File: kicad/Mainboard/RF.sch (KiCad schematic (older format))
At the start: 97 parts, among them J7 Antenna, T1 AFT05MS004NT1, U5 HMC546MS8GETR

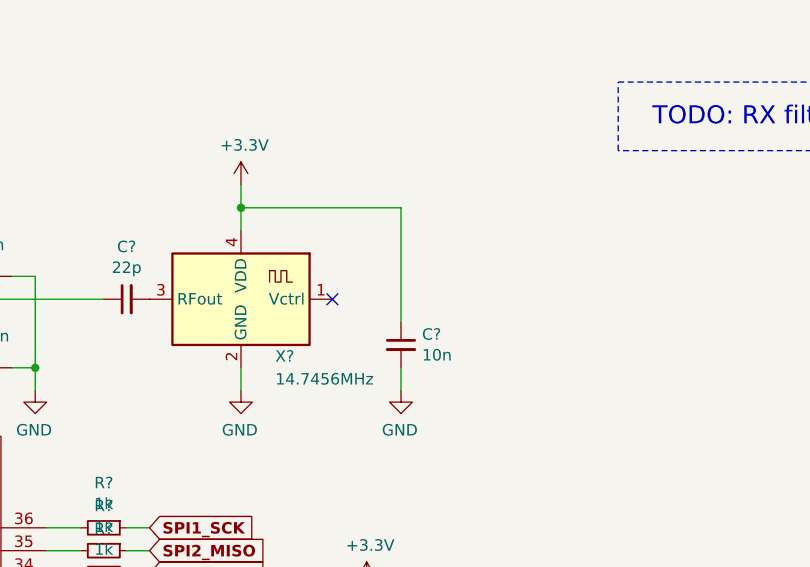
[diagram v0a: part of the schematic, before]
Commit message: Add files via upload
replaced TCXO with ECS-TXO-3225-122.8-TR
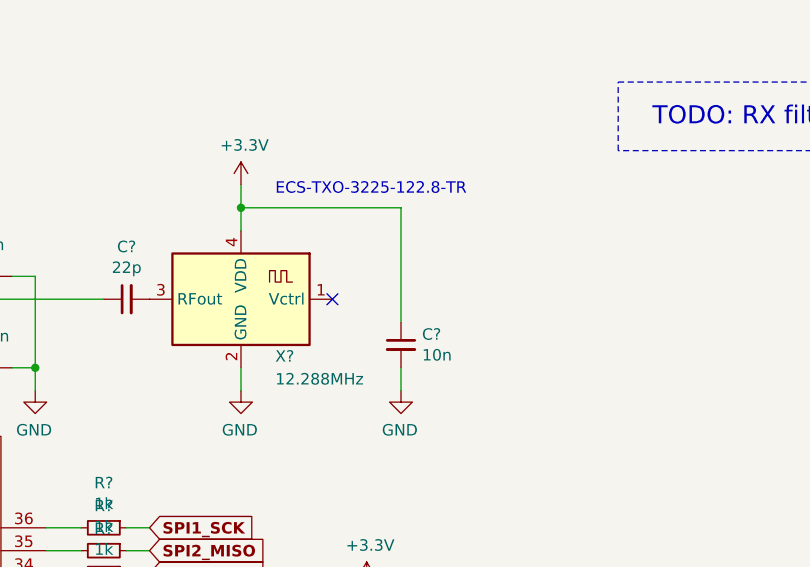
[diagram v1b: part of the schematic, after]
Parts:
- X?: value 14.7456MHz -> 12.288MHz; footprint Oscillator:Oscillator_SMD_Abracon_ABLNO -> (none)
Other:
- note added: "ECS-TXO-3225-122.8-TR"
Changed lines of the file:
@@
 P 7100 7250
 F 0 "X?" H 6950 7000 50  0000 R CNN
-F 1 "14.7456MHz" H 6950 6900 50  0000 R CNN
-F 2 "Oscillator:Oscillator_SMD_Abracon_ABLNO" H 7100 6900 50  0001 C CNN
-F 3 "https://abracon.com/Precisiontiming/ABLNO.pdf" H 6900 7350 50  0001 C CNN
+F 1 "12.288MHz" H 6950 6900 50  0000 R CNN
+F 2 "" H 7100 6900 50  0001 C CNN
+F 3 "" H 6900 7350 50  0001 C CNN
 	1    7100 7250
 	-1   0    0    -1
@@
 Text GLabel 6700 8450 2    50   Input ~ 10
 SPI2_MOSI
+Text Notes 7250 6800 0    50   ~ 0
+ECS-TXO-3225-122.8-TR
 $EndSCHEMATC

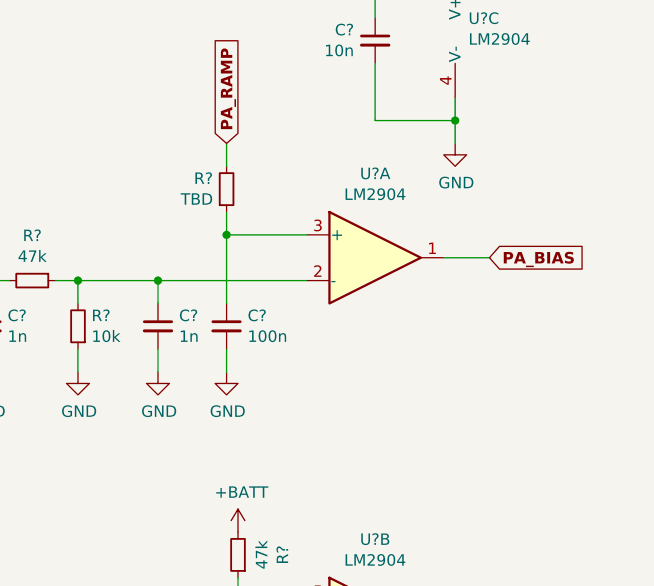
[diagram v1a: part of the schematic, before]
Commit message: Add files via upload
added a resistor to form a voltage divider network (at pin 3 of LM2904) and changed the cap from 100n to 10n
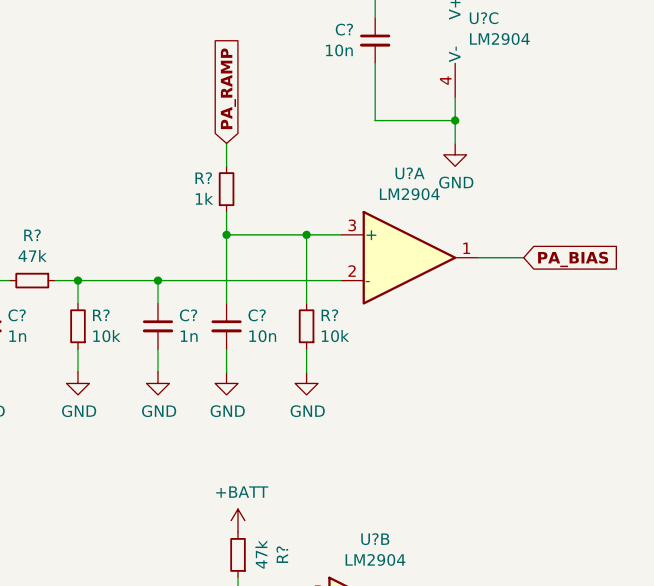
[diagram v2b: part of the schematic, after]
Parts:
- added R?: 10k, symbol Device:R_Small
- C?: value 100n -> 10n
- R?: value TBD -> 1k
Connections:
- net GND: now also R?.1
- net at C?.1, R?.1, U?.3 (+): now also R?.2
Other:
- moved on the sheet: U?A
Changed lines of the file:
@@
 Text GLabel 7600 4450 0    50   Input ~ 10
 RX
-Text GLabel 14400 4300 2    50   Input ~ 10
+Text GLabel 14550 4300 2    50   Input ~ 10
 PA_BIAS
 Wire Wire Line
@@
 L Amplifier_Operational:LM2904 U?
 U 1 1 5E1834DE
-P 13900 4300
-F 0 "U?" H 13900 4667 50  0000 C CNN
-F 1 "LM2904" H 13900 4576 50  0000 C CNN
-F 2 "" H 13900 4300 50  0001 C CNN
-F 3 "http://www.ti.com/lit/ds/symlink/lm358.pdf" H 13900 4300 50  0001 C CNN
-	1    13900 4300
+P 14050 4300
+F 0 "U?" H 14050 4667 50  0000 C CNN
+F 1 "LM2904" H 14050 4576 50  0000 C CNN
+F 2 "" H 14050 4300 50  0001 C CNN
+F 3 "http://www.ti.com/lit/ds/symlink/lm358.pdf" H 14050 4300 50  0001 C CNN
+	1    14050 4300
 	1    0    0    -1
 $EndComp
@@
 P 13250 4600
 F 0 "C?" H 13342 4646 50  0000 L CNN
-F 1 "100n" H 13342 4555 50  0000 L CNN
+F 1 "10n" H 13342 4555 50  0000 L CNN
 F 2 "" H 13250 4600 50  0001 C CNN
 F 3 "~" H 13250 4600 50  0001 C CNN
@@
 $EndComp
 Wire Wire Line
-	12950 4400 13600 4400
-Wire Wire Line
 	13250 4500 13250 4200
-Wire Wire Line
-	13250 4200 13600 4200
 $Comp
 L power:GND #PWR?
@@
 P 13250 4000
 F 0 "R?" H 13191 3954 50  0000 R CNN
-F 1 "TBD" H 13191 4045 50  0000 R CNN
+F 1 "1k" H 13191 4045 50  0000 R CNN
 F 2 "" H 13250 4000 50  0001 C CNN
 F 3 "~" H 13250 4000 50  0001 C CNN
@@
 $EndComp
 Wire Wire Line
-	14200 4300 14400 4300
+	14350 4300 14550 4300
 $Comp
 L adf7021:ADF7021 U?
@@
 Text Notes 7250 6800 0    50   ~ 0
 ECS-TXO-3225-122.8-TR
+$Comp
+L Device:R_Small R?
+U 1 1 5E30B1F2
+P 13600 4600
+F 0 "R?" H 13541 4554 50  0000 R CNN
+F 1 "10k" H 13541 4645 50  0000 R CNN
+F 2 "" H 13600 4600 50  0001 C CNN
+F 3 "~" H 13600 4600 50  0001 C CNN
+	1    13600 4600
+	-1   0    0    1
+$EndComp
+Wire Wire Line
+	13250 4200 13600 4200
+Wire Wire Line
+	13600 4700 13600 4800
+$Comp
+L power:GND #PWR?
+U 1 1 5E38C57C
+P 13600 4800
+F 0 "#PWR?" H 13600 4550 50  0001 C CNN
+F 1 "GND" H 13605 4627 50  0000 C CNN
+F 2 "" H 13600 4800 50  0001 C CNN
+F 3 "" H 13600 4800 50  0001 C CNN
+	1    13600 4800
+	1    0    0    -1
+$EndComp
+Wire Wire Line
+	12950 4400 13600 4400
+Connection ~ 13600 4200
+Wire Wire Line
+	13600 4200 13750 4200
+Wire Wire Line
+	13600 4400 13750 4400
+Wire Wire Line
+	13600 4200 13600 4500
 $EndSCHEMATC

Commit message: Annotated parts, again.
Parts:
- gave numbers to parts that had none: 71
- renumbered C31 to C42, C38 to C43, C21 to C47, C22 to C48, C24 to C49, C30 to C51, C25 to C52, C32 to C53, C26 to C54, C33 to C55, C28 to C57, C43 to C58, C41 to C61, C35 to C63, C39 to C64, C40 to C67, J7 to J8, L4 to L10, L10 to L13, L9 to L7, L2 to L8, L3 to L9, R9 to R18, U5 to U6

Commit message: Started assigning footprints
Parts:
- C21, C22, C23, C24, C25, C26, C27, C28, C29, C30, C31, C32, C33, C35, C36, C37, C38, C39, C40, C41, C44, C45, C46, C50, C56, C59, C60, C62, C65, C66, C68, C69, C70, C71: footprint (none) -> Capacitor_SMD:C_0603_1608Metric; symbol Device:C_Small -> Mainboard-rescue:C_Small-Device
- C34: footprint (none) -> Capacitor_SMD:C_0603_1608Metric; symbol Device:CP_Small -> Mainboard-rescue:CP_Small-Device
- C42, C43, C48, C49, C51, C52, C53, C54, C55, C57, C58, C61, C63, C64, C67: footprint (none) -> Capacitor_SMD:C_0603_1608Metric
- C47: footprint (none) -> Capacitor_Tantalum_SMD:CP_EIA-3216-18_Kemet-A; Partno (none) -> T491A105M016AT
- D2: footprint (none) -> Package_TO_SOT_SMD:SOT-23; symbol Device:D_x2_KCom_AAK -> Mainboard-rescue:D_x2_KCom_AAK-Device
- L11, L12, L2, L3, L4, L6: symbol Device:L_Small -> Mainboard-rescue:L_Small-Device
- L5: footprint (none) -> Inductor_SMD:L_0603_1608Metric; symbol Device:L_Small -> Mainboard-rescue:L_Small-Device
- R10, R11, R12, R13, R14, R15, R16, R17, R19, R20, R21, R22, R23, R24, R25, R26, R27, R28, R29, R8, R9: symbol Device:R_Small -> Mainboard-rescue:R_Small-Device
- TP1, TP2, TP3: symbol Connector:TestPoint_Probe -> Mainboard-rescue:TestPoint_Probe-Connector
- U7: symbol Amplifier_Operational:LM2904 -> Mainboard-rescue:LM2904-Amplifier_Operational
- X1: symbol Oscillator:ABLNO -> Mainboard-rescue:ABLNO-Oscillator

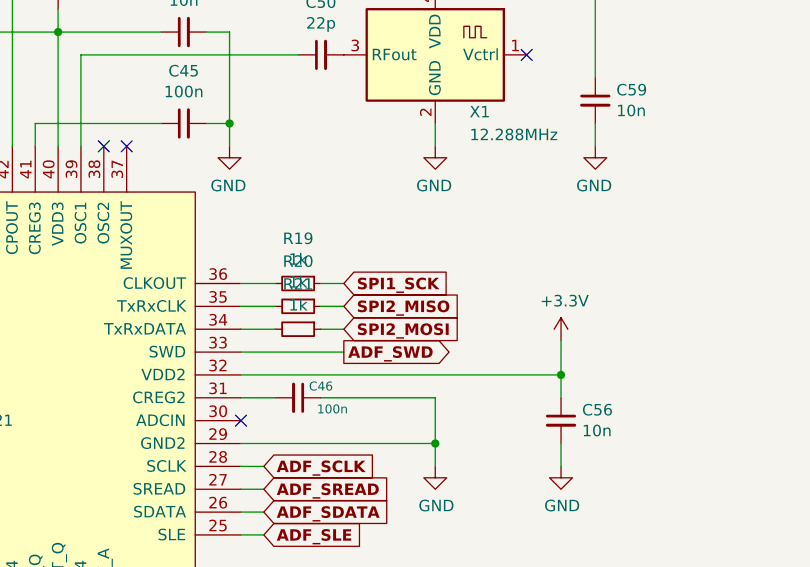
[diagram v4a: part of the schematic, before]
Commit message: Add files via upload
ADF7021 pin 36: SPI1_SCK -> SPI2_SCK
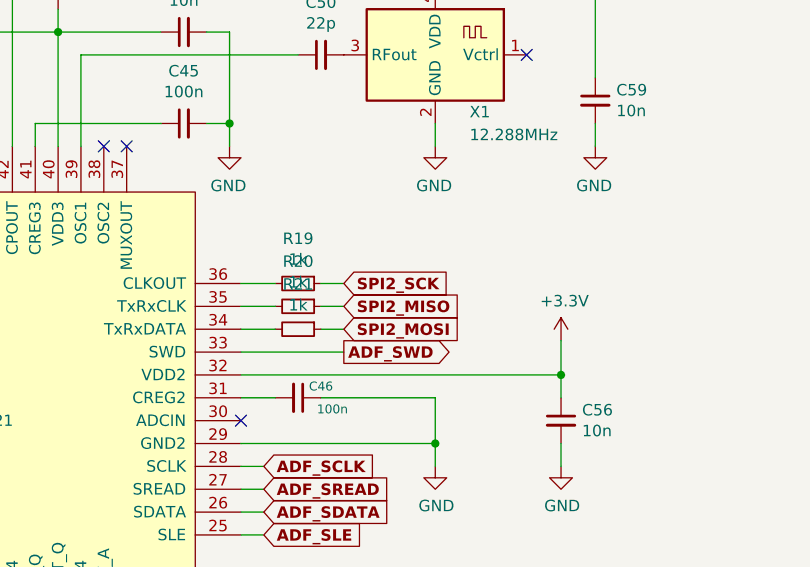
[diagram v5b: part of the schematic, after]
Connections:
- net SPI1_SCK renamed SPI2_SCK
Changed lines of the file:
@@
 EESchema Schematic File Version 4
+LIBS:Mainboard-cache
 EELAYER 30 0
 EELAYER END
@@
 	13300 5800 13600 5800
 Text GLabel 6700 8250 2    50   Input ~ 10
-SPI1_SCK
+SPI2_SCK
 Text GLabel 6700 8350 2    50   Input ~ 10
 SPI2_MISO

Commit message: Add files via upload
assigned some more footprints
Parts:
- L10, L11, L12, L13, L2, L3, L4, L6, L7, L9: footprint (none) -> Inductor_SMD:L_0603_1608Metric
- R10, R11, R12, R13, R14, R15, R16, R17, R18, R19, R20, R21, R22, R23, R24, R25, R26, R27, R28, R29, R8, R9: footprint (none) -> Resistor_SMD:R_0603_1608Metric
- TP1, TP2, TP3: footprint (none) -> TestPoint:TestPoint_Pad_D1.0mm
- U5: footprint (none) -> Package_CSP:LFCSP-48-1EP_7x7mm_P0.5mm_EP4.1x4.1mm_ThermalVias
- U6: footprint (none) -> Package_SO:MSOP-8-1EP_3x3mm_P0.65mm_EP2.5x3mm_Mask1.73x2.36mm_ThermalVias
- U7: footprint (none) -> Package_SO:SO-8_3.9x4.9mm_P1.27mm
- U7: value LM2904 -> LM2904A; footprint (none) -> Package_SO:SO-8_3.9x4.9mm_P1.27mm
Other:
- note removed: "Coilcraft 0402CS series inductor, 5%"
- note removed: "Toko LL1005-FH series inductor, 5%"
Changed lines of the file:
@@
 F 0 "L7" V 5885 3000 50  0000 C CNN
 F 1 "2.7nH" V 5794 3000 50  0000 C CNN
-F 2 "" H 5700 3000 50  0001 C CNN
+F 2 "Inductor_SMD:L_0603_1608Metric" H 5700 3000 50  0001 C CNN
 F 3 "~" H 5700 3000 50  0001 C CNN
 	1    5700 3000
@@
 F 0 "R18" H 5959 2846 50  0000 L CNN
 F 1 "6k8" H 5959 2755 50  0000 L CNN
-F 2 "" H 5900 2800 50  0001 C CNN
+F 2 "Resistor_SMD:R_0603_1608Metric" H 5900 2800 50  0001 C CNN
 F 3 "~" H 5900 2800 50  0001 C CNN
 	1    5900 2800
@@
 F 0 "L9" V 7185 2500 50  0000 C CNN
 F 1 "1nH" V 7094 2500 50  0000 C CNN
-F 2 "" H 7000 2500 50  0001 C CNN
+F 2 "Inductor_SMD:L_0603_1608Metric" H 7000 2500 50  0001 C CNN
 F 3 "~" H 7000 2500 50  0001 C CNN
 	1    7000 2500
@@
 F 0 "L10" V 7585 2500 50  0000 C CNN
 F 1 "1nH" V 7494 2500 50  0000 C CNN
-F 2 "" H 7400 2500 50  0001 C CNN
+F 2 "Inductor_SMD:L_0603_1608Metric" H 7400 2500 50  0001 C CNN
 F 3 "~" H 7400 2500 50  0001 C CNN
 	1    7400 2500
@@
 F 0 "U6" H 9500 3500 50  0000 C CNN
 F 1 "HMC546MS8GETR" H 9750 3400 50  0000 C CNN
-F 2 "" H 9550 3000 50  0001 C CNN
+F 2 "Package_SO:MSOP-8-1EP_3x3mm_P0.65mm_EP2.5x3mm_Mask1.73x2.36mm_ThermalVias" H 9550 3000 50  0001 C CNN
 F 3 "" H 9550 3000 50  0001 C CNN
 	1    9550 3000
@@
 F 0 "L12" V 9485 4450 50  0000 C CNN
 F 1 "15nH" V 9394 4450 50  0000 C CNN
-F 2 "" H 9300 4450 50  0001 C CNN
+F 2 "Inductor_SMD:L_0603_1608Metric" H 9300 4450 50  0001 C CNN
 F 3 "~" H 9300 4450 50  0001 C CNN
 	1    9300 4450
@@
 F 0 "L11" V 9485 2150 50  0000 C CNN
 F 1 "100nH" V 9394 2150 50  0000 C CNN
-F 2 "" H 9300 2150 50  0001 C CNN
+F 2 "Inductor_SMD:L_0603_1608Metric" H 9300 2150 50  0001 C CNN
 F 3 "~" H 9300 2150 50  0001 C CNN
 	1    9300 2150
@@
 Wire Wire Line
 	10250 2150 10250 3000
-Text Notes 8600 4550 0    50   ~ 0
-Coilcraft 0402CS series inductor, 5%
-Text Notes 8600 2250 0    50   ~ 0
-Toko LL1005-FH series inductor, 5%
 Wire Wire Line
 	10650 3300 10650 3400
@@
 F 0 "L13" V 11185 3000 50  0000 C CNN
 F 1 "15nH" V 11094 3000 50  0000 C CNN
-F 2 "" H 11000 3000 50  0001 C CNN
+F 2 "Inductor_SMD:L_0603_1608Metric" H 11000 3000 50  0001 C CNN
 F 3 "~" H 11000 3000 50  0001 C CNN
 	1    11000 3000
@@
 F 0 "R22" H 10741 5104 50  0000 R CNN
 F 1 "33k" H 10741 5195 50  0000 R CNN
-F 2 "" H 10800 5150 50  0001 C CNN
+F 2 "Resistor_SMD:R_0603_1608Metric" H 10800 5150 50  0001 C CNN
 F 3 "~" H 10800 5150 50  0001 C CNN
 	1    10800 5150
@@
 F 0 "R23" H 11141 5104 50  0000 R CNN
 F 1 "33k" H 11141 5195 50  0000 R CNN
-F 2 "" H 11200 5150 50  0001 C CNN
+F 2 "Resistor_SMD:R_0603_1608Metric" H 11200 5150 50  0001 C CNN
 F 3 "~" H 11200 5150 50  0001 C CNN
 	1    11200 5150
@@
 F 0 "R24" V 12204 4400 50  0000 C CNN
 F 1 "47k" V 12295 4400 50  0000 C CNN
-F 2 "" H 12400 4400 50  0001 C CNN
+F 2 "Resistor_SMD:R_0603_1608Metric" H 12400 4400 50  0001 C CNN
 F 3 "~" H 12400 4400 50  0001 C CNN
 	1    12400 4400
@@
 F 0 "R25" H 12541 4554 50  0000 R CNN
 F 1 "10k" H 12541 4645 50  0000 R CNN
-F 2 "" H 12600 4600 50  0001 C CNN
+F 2 "Resistor_SMD:R_0603_1608Metric" H 12600 4600 50  0001 C CNN
 F 3 "~" H 12600 4600 50  0001 C CNN
 	1    12600 4600
@@
 F 0 "U7" H 14308 3346 50  0000 L CNN
 F 1 "LM2904" H 14308 3255 50  0000 L CNN
-F 2 "" H 14350 3300 50  0001 C CNN
+F 2 "Package_SO:SO-8_3.9x4.9mm_P1.27mm" H 14350 3300 50  0001 C CNN
 F 3 "http://www.ti.com/lit/ds/symlink/lm358.pdf" H 14350 3300 50  0001 C CNN
 	3    14350 3300
@@
 U 1 1 5E1834DE
 P 14050 4300
-F 0 "U7" H 14050 4667 50  0000 C CNN
-F 1 "LM2904" H 14050 4576 50  0000 C CNN
-F 2 "" H 14050 4300 50  0001 C CNN
+F 0 "U7" H 14200 4100 50  0000 C CNN
+F 1 "LM2904A" H 14200 4000 50  0000 C CNN
+F 2 "Package_SO:SO-8_3.9x4.9mm_P1.27mm" H 14050 4300 50  0001 C CNN
 F 3 "http://www.ti.com/lit/ds/symlink/lm358.pdf" H 14050 4300 50  0001 C CNN
 	1    14050 4300
@@
 F 0 "U7" H 13900 6267 50  0000 C CNN
 F 1 "LM2904" H 13900 6176 50  0000 C CNN
-F 2 "" H 13900 5900 50  0001 C CNN
+F 2 "Package_SO:SO-8_3.9x4.9mm_P1.27mm" H 13900 5900 50  0001 C CNN
 F 3 "http://www.ti.com/lit/ds/symlink/lm358.pdf" H 13900 5900 50  0001 C CNN
 	2    13900 5900
@@
 F 0 "R26" H 13191 3954 50  0000 R CNN
 F 1 "1k" H 13191 4045 50  0000 R CNN
-F 2 "" H 13250 4000 50  0001 C CNN
+F 2 "Resistor_SMD:R_0603_1608Metric" H 13250 4000 50  0001 C CNN
 F 3 "~" H 13250 4000 50  0001 C CNN
 	1    13250 4000
@@
 F 0 "U5" H 5100 8850 49  0000 C CNN
 F 1 "ADF7021" H 5100 8750 49  0000 C CNN
-F 2 "" H 4900 8550 49  0001 C CNN
+F 2 "Package_CSP:LFCSP-48-1EP_7x7mm_P0.5mm_EP4.1x4.1mm_ThermalVias" H 4900 8550 49  0001 C CNN
 F 3 "" H 4900 8550 49  0001 C CNN
 	1    5100 8800
@@
 F 0 "R11" H 3459 9696 50  0000 L CNN
 F 1 "3k6" H 3459 9605 50  0000 L CNN
-F 2 "" H 3400 9650 50  0001 C CNN
+F 2 "Resistor_SMD:R_0603_1608Metric" H 3400 9650 50  0001 C CNN
 F 3 "~" H 3400 9650 50  0001 C CNN
 	1    3400 9650
@@
 F 0 "R9" H 2859 9696 50  0000 L CNN
 F 1 "1k1" H 2859 9605 50  0000 L CNN
-F 2 "" H 2800 9650 50  0001 C CNN
+F 2 "Resistor_SMD:R_0603_1608Metric" H 2800 9650 50  0001 C CNN
 F 3 "~" H 2800 9650 50  0001 C CNN
 	1    2800 9650
@@
 F 0 "L4" V 2450 8900 50  0000 L CNN
 F 1 "27n" V 2600 8900 50  0000 L CNN
-F 2 "" H 2500 8950 50  0001 C CNN
+F 2 "Inductor_SMD:L_0603_1608Metric" H 2500 8950 50  0001 C CNN
 F 3 "~" H 2500 8950 50  0001 C CNN
 	1    2500 8950
@@
 F 0 "L3" V 2450 8300 50  0000 L CNN
 F 1 "15n" V 2600 8300 50  0000 L CNN
-F 2 "" H 2500 8350 50  0001 C CNN
+F 2 "Inductor_SMD:L_0603_1608Metric" H 2500 8350 50  0001 C CNN
 F 3 "~" H 2500 8350 50  0001 C CNN
 	1    2500 8350
@@
 F 0 "R12" V 3404 7150 50  0000 C CNN
 F 1 "3R9" V 3495 7150 50  0000 C CNN
-F 2 "" H 3600 7150 50  0001 C CNN
+F 2 "Resistor_SMD:R_0603_1608Metric" H 3600 7150 50  0001 C CNN
 F 3 "~" H 3600 7150 50  0001 C CNN
 	1    3600 7150
@@
 F 0 "R15" H 4509 6146 50  0000 L CNN
 F 1 "560" H 4509 6055 50  0000 L CNN
-F 2 "" H 4450 6100 50  0001 C CNN
+F 2 "Resistor_SMD:R_0603_1608Metric" H 4450 6100 50  0001 C CNN
 F 3 "~" H 4450 6100 50  0001 C CNN
 	1    4450 6100
@@
 F 0 "R17" H 4809 6146 50  0000 L CNN
 F 1 "270" H 4809 6055 50  0000 L CNN
-F 2 "" H 4750 6100 50  0001 C CNN
+F 2 "Resistor_SMD:R_0603_1608Metric" H 4750 6100 50  0001 C CNN
 F 3 "~" H 4750 6100 50  0001 C CNN
 	1    4750 6100
@@
 F 0 "L2" V 2485 3000 50  0000 C CNN
 F 1 "20n" V 2394 3000 50  0000 C CNN
-F 2 "" H 2300 3000 50  0001 C CNN
+F 2 "Inductor_SMD:L_0603_1608Metric" H 2300 3000 50  0001 C CNN
 F 3 "~" H 2300 3000 50  0001 C CNN
 	1    2300 3000
@@
 F 0 "L6" H 4648 2846 50  0000 L CNN
 F 1 "68nH" H 4648 2755 50  0000 L CNN
-F 2 "" H 4600 2800 50  0001 C CNN
+F 2 "Inductor_SMD:L_0603_1608Metric" H 4600 2800 50  0001 C CNN
 F 3 "~" H 4600 2800 50  0001 C CNN
 	1    4600 2800
@@
 F 0 "R16" H 4541 1304 50  0000 R CNN
 F 1 "51" H 4541 1395 50  0000 R CNN
-F 2 "" H 4600 1350 50  0001 C CNN
+F 2 "Resistor_SMD:R_0603_1608Metric" H 4600 1350 50  0001 C CNN
 F 3 "~" H 4600 1350 50  0001 C CNN
 	1    4600 1350
@@
 F 0 "R19" V 6304 8250 50  0000 C CNN
 F 1 "1k" V 6395 8250 50  0000 C CNN
-F 2 "" H 6500 8250 50  0001 C CNN
+F 2 "Resistor_SMD:R_0603_1608Metric" H 6500 8250 50  0001 C CNN
 F 3 "~" H 6500 8250 50  0001 C CNN
 	1    6500 8250
@@
 F 0 "R20" V 6304 8350 50  0000 C CNN
 F 1 "1k" V 6395 8350 50  0000 C CNN
-F 2 "" H 6500 8350 50  0001 C CNN
+F 2 "Resistor_SMD:R_0603_1608Metric" H 6500 8350 50  0001 C CNN
 F 3 "~" H 6500 8350 50  0001 C CNN
 	1    6500 8350
@@
 F 0 "R21" V 6304 8450 50  0000 C CNN
 F 1 "1k" V 6395 8450 50  0000 C CNN
-F 2 "" H 6500 8450 50  0001 C CNN
+F 2 "Resistor_SMD:R_0603_1608Metric" H 6500 8450 50  0001 C CNN
 F 3 "~" H 6500 8450 50  0001 C CNN
 	1    6500 8450
@@
 F 0 "R14" V 4004 6300 50  0000 C CNN
 F 1 "100" V 4095 6300 50  0000 C CNN
-F 2 "" H 4200 6300 50  0001 C CNN
+F 2 "Resistor_SMD:R_0603_1608Metric" H 4200 6300 50  0001 C CNN
 F 3 "~" H 4200 6300 50  0001 C CNN
 	1    4200 6300
@@
 F 0 "R13" V 3554 6300 50  0000 C CNN
 F 1 "47k" V 3645 6300 50  0000 C CNN
-F 2 "" H 3750 6300 50  0001 C CNN
+F 2 "Resistor_SMD:R_0603_1608Metric" H 3750 6300 50  0001 C CNN
 F 3 "~" H 3750 6300 50  0001 C CNN
 	1    3750 6300
@@
 F 0 "TP2" H 4603 6401 50  0000 L CNN
 F 1 "TestPoint_Probe" H 4603 6310 50  0000 L CNN
-F 2 "" H 4650 6300 50  0001 C CNN
+F 2 "TestPoint:TestPoint_Pad_D1.0mm" H 4650 6300 50  0001 C CNN
 F 3 "~" H 4650 6300 50  0001 C CNN
 	1    4450 6300
@@
 F 0 "TP1" H 4153 6901 50  0000 L CNN
 F 1 "TestPoint_Probe" H 4153 6810 50  0000 L CNN
-F 2 "" H 4200 6800 50  0001 C CNN
+F 2 "TestPoint:TestPoint_Pad_D1.0mm" H 4200 6800 50  0001 C CNN
 F 3 "~" H 4200 6800 50  0001 C CNN
 	1    4000 6800
@@
 F 0 "TP3" H 5403 6401 50  0000 L CNN
 F 1 "TestPoint_Probe" H 5403 6310 50  0000 L CNN
-F 2 "" H 5450 6300 50  0001 C CNN
+F 2 "TestPoint:TestPoint_Pad_D1.0mm" H 5450 6300 50  0001 C CNN
 F 3 "~" H 5450 6300 50  0001 C CNN
 	1    5250 6300
@@
 F 0 "R8" V 2454 6450 50  0000 C CNN
 F 1 "22k" V 2545 6450 50  0000 C CNN
-F 2 "" H 2650 6450 50  0001 C CNN
+F 2 "Resistor_SMD:R_0603_1608Metric" H 2650 6450 50  0001 C CNN
 F 3 "~" H 2650 6450 50  0001 C CNN
 	1    2650 6450
@@
 F 0 "R10" V 2754 6300 50  0000 C CNN
 F 1 "47k" V 2845 6300 50  0000 C CNN
-F 2 "" H 2950 6300 50  0001 C CNN
+F 2 "Resistor_SMD:R_0603_1608Metric" H 2950 6300 50  0001 C CNN
 F 3 "~" H 2950 6300 50  0001 C CNN
 	1    2950 6300
@@
 F 0 "R27" V 13104 5600 50  0000 C CNN
 F 1 "47k" V 13195 5600 50  0000 C CNN
-F 2 "" H 13300 5600 50  0001 C CNN
+F 2 "Resistor_SMD:R_0603_1608Metric" H 13300 5600 50  0001 C CNN
 F 3 "~" H 13300 5600 50  0001 C CNN
 	1    13300 5600
@@
 F 0 "R28" V 13104 6200 50  0000 C CNN
 F 1 "47k" V 13195 6200 50  0000 C CNN
-F 2 "" H 13300 6200 50  0001 C CNN
+F 2 "Resistor_SMD:R_0603_1608Metric" H 13300 6200 50  0001 C CNN
 F 3 "~" H 13300 6200 50  0001 C CNN
 	1    13300 6200
@@
 F 0 "R29" H 13541 4554 50  0000 R CNN
 F 1 "10k" H 13541 4645 50  0000 R CNN
-F 2 "" H 13600 4600 50  0001 C CNN
+F 2 "Resistor_SMD:R_0603_1608Metric" H 13600 4600 50  0001 C CNN
 F 3 "~" H 13600 4600 50  0001 C CNN
 	1    13600 4600
